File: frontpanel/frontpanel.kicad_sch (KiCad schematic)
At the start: 2 parts

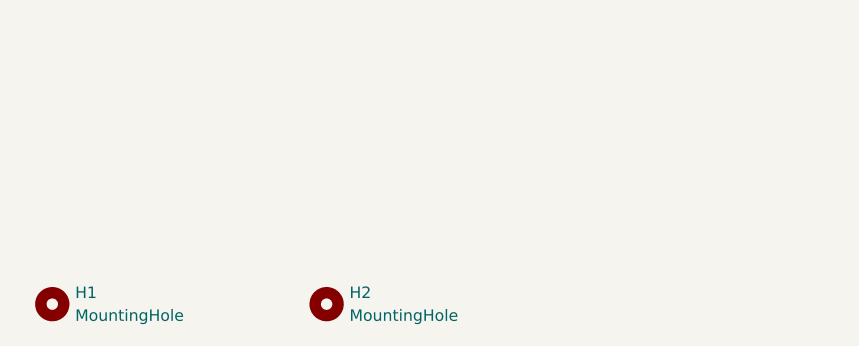
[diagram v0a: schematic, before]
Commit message: frontpanel functional, CV input GND added
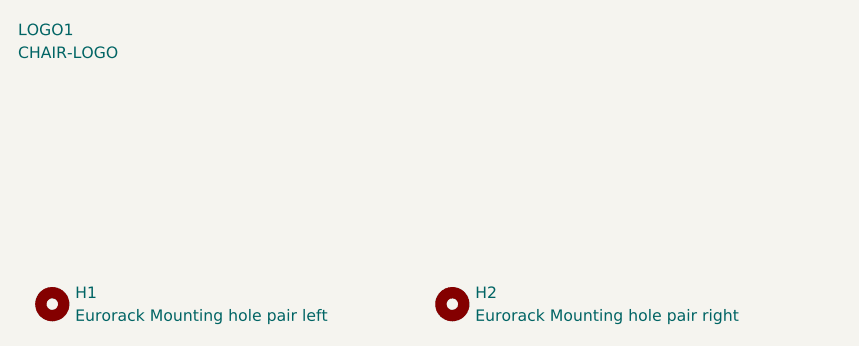
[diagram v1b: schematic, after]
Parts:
- added LOGO1: CHAIR-LOGO, CHAIR:CHAIR_logo_silkscreen, symbol CHAIR:CHAIR-LOGO
- H1: value MountingHole -> Eurorack Mounting hole pair left
- H2: value MountingHole -> Eurorack Mounting hole pair right
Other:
- moved on the sheet: H2
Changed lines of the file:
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@@
       (effects (font (size 1.27 1.27)) (justify left))
     )
-    (property "Value" "MountingHole" (id 1) (at 82.55 60.9599 0)
+    (property "Value" "Eurorack Mounting hole pair left" (id 1) (at 82.55 60.9599 0)
       (effects (font (size 1.27 1.27)) (justify left))
     )
@@
     )
   )
-  (symbol (lib_id "CHAIR:MountingHole") (at 110.49 59.69 0) (unit 1)
+  (symbol (lib_id "CHAIR:CHAIR-LOGO") (at 74.93 30.48 0) (unit 1)
     (in_bom no) (on_board yes) (fields_autoplaced)
-    (property "Reference" "H2" (id 0) (at 113.03 58.4199 0)
+    (property "Reference" "LOGO1" (id 0) (at 76.2 29.2099 0)
       (effects (font (size 1.27 1.27)) (justify left))
     )
-    (property "Value" "MountingHole" (id 1) (at 113.03 60.9599 0)
+    (property "Value" "CHAIR-LOGO" (id 1) (at 76.2 31.7499 0)
       (effects (font (size 1.27 1.27)) (justify left))
     )
-    (property "Footprint" "CHAIR:MountingHole_Eurorack_3U_slotted" (id 2) (at 110.49 59.69 0)
+    (property "Footprint" "CHAIR:CHAIR_logo_silkscreen" (id 2) (at 74.93 33.02 0)
       (effects (font (size 1.27 1.27)) hide)
     )
-    (property "Datasheet" "~" (id 3) (at 110.49 59.69 0)
+    (property "Datasheet" "" (id 3) (at 74.93 30.48 0)
+      (effects (font (size 1.27 1.27)) hide)
+    )
+  )
+  (symbol (lib_id "CHAIR:MountingHole") (at 124.46 59.69 0) (unit 1)
+    (in_bom no) (on_board yes) (fields_autoplaced)
+    (property "Reference" "H2" (id 0) (at 127 58.4199 0)
+      (effects (font (size 1.27 1.27)) (justify left))
+    )
+    (property "Value" "Eurorack Mounting hole pair right" (id 1) (at 127 60.9599 0)
+      (effects (font (size 1.27 1.27)) (justify left))
+    )
+    (property "Footprint" "CHAIR:MountingHole_Eurorack_3U_slotted" (id 2) (at 124.46 59.69 0)
+      (effects (font (size 1.27 1.27)) hide)
+    )
+    (property "Datasheet" "~" (id 3) (at 124.46 59.69 0)
       (effects (font (size 1.27 1.27)) hide)
     )
@@
   (symbol_instances
     (path "/58961c6d-825c-484a-9d59-20734fae15e4"
-      (reference "H1") (unit 1) (value "MountingHole") (footprint "CHAIR:MountingHole_Eurorack_3U_slotted")
+      (reference "H1") (unit 1) (value "Eurorack Mounting hole pair left") (footprint "CHAIR:MountingHole_Eurorack_3U_slotted")
     )
     (path "/89153324-5a8f-450b-8850-83b24e8396da"
-      (reference "H2") (unit 1) (value "MountingHole") (footprint "CHAIR:MountingHole_Eurorack_3U_slotted")
+      (reference "H2") (unit 1) (value "Eurorack Mounting hole pair right") (footprint "CHAIR:MountingHole_Eurorack_3U_slotted")
+    )
+    (path "/68573cd7-b5e0-45a0-b20d-ec0846befa25"
+      (reference "LOGO1") (unit 1) (value "CHAIR-LOGO") (footprint "CHAIR:CHAIR_logo_silkscreen")
     )
   )
